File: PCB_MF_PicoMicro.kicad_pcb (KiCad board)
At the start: 2 copper layers, 38 x 18.5 mm, 32 parts, among them J2 Conn_01x02_Pin, J3 USB_C_Receptacle_USB2.0_16P, J7 Conn_01x02_Pin, J8 Conn_01x02_Pin, U1 RP2040, U2 AMS1117-3.3, U4 W25Q16JVSS, U5 ProMicro, Y1 X322512MSB4SI

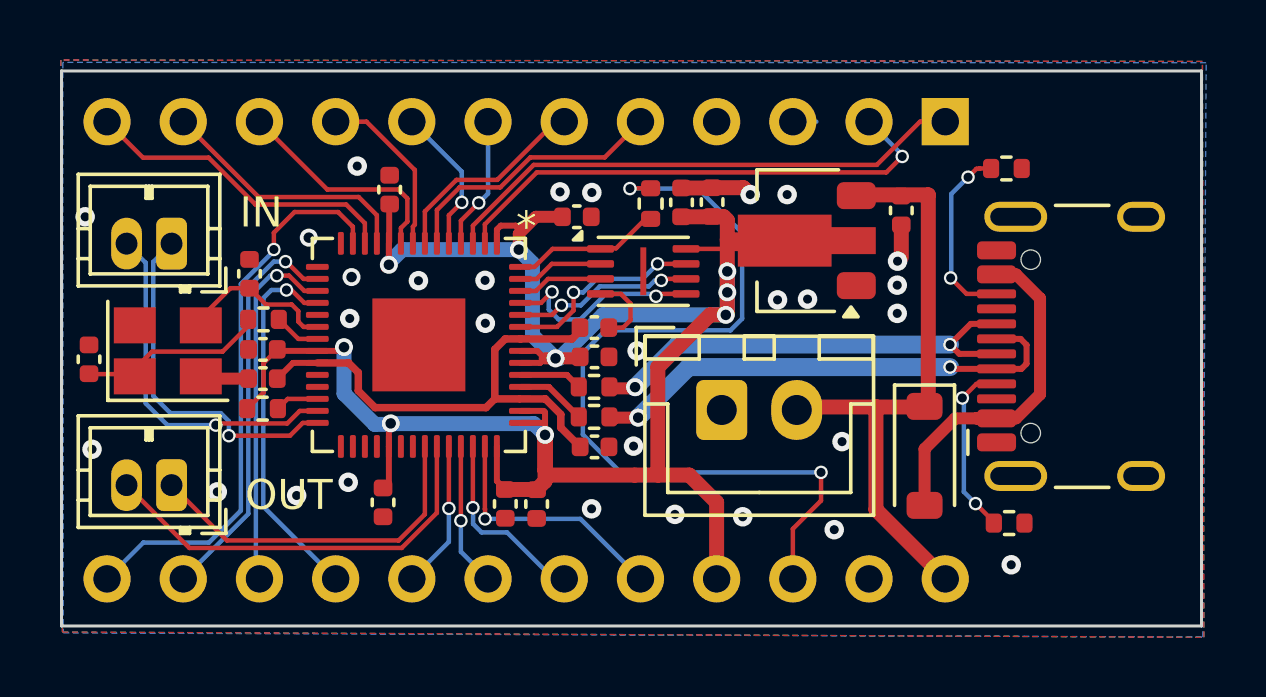
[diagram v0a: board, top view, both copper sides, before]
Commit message: first changes for RP2350A
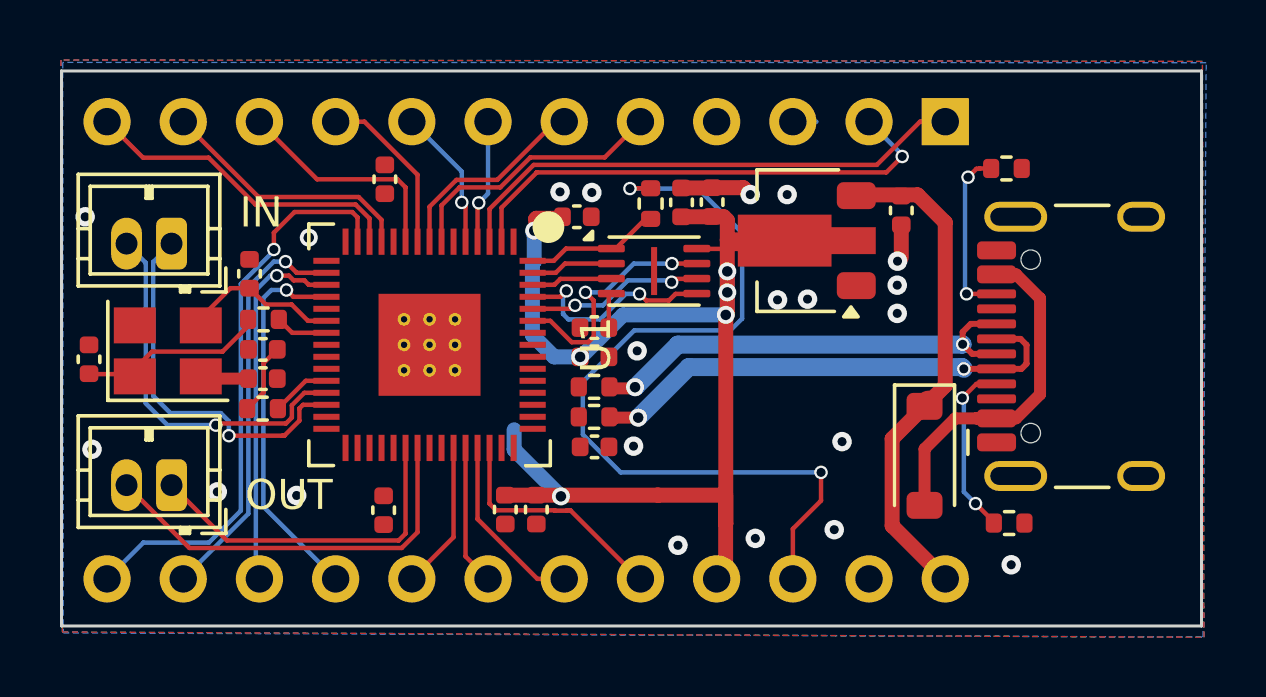
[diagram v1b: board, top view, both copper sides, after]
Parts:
- removed J2: Conn_01x02_Pin, Connector_JST:JST_XH_B2B-XH-A_1x02_P2.50mm_Vertical
- U1: footprint _Neil:QFN56P40_700X700X90L40X18T310N -> _Own_Library:RP2350A_QFN-60_EP_7.75x7.75_Pitch0.4mm
- moved C13 0.38 mm to (116.0, 85.0)
- moved U4 0.36 mm to (125.0, 88.1)
- moved U1 0.36 mm to (117.5, 90.5), turned to -90 degrees
- moved C11 0.26 mm to (116.0, 96.1)
- moved C9 0.19 mm to (120.0, 96.0)
- moved C10 0.18 mm to (121.1, 96.0)
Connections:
- U1 pad 10: 3.3V -> D7
- U1 pad 11: D8 -> 3.3V
- U1 pad 12: D9 -> D8
- U1 pad 13: D10 -> D9
- U1 pad 14: /RP2040/GPIO11 -> D10
- U1 pad 15: /RP2040/GPIO12 -> /RP2040/GPIO11
- U1 pad 16: D13 -> /RP2040/GPIO12
- U1 pad 17: D14 -> D13
- U1 pad 18: D15 -> D14
- U1 pad 19: GND -> D15
- U1 pad 20: /RP2040/XIN -> 3.3V
- U1 pad 21: /RP2040/XOUT_R -> /RP2040/XIN
- U1 pad 22: 3.3V -> /RP2040/XOUT_R
- U1 pad 30: /RP2040/GPIO19 -> 3.3V
- U1 pad 31: /RP2040/GPIO20 -> /RP2040/GPIO19
- U1 pad 32: /RP2040/GPIO21 -> /RP2040/GPIO20
- U1 pad 33: 3.3V -> /RP2040/GPIO21
- U1 pad 38: A0 -> 3.3V
- U1 pad 39: A1 -> +1V1
- U1 pad 40: A2 -> A0
- U1 pad 41: A3 -> A1
- U1 pad 42: 3.3V -> A2
- U1 pad 43: 3.3V -> A3
- U1 pad 45: +1V1 -> 3.3V
- U1 pad 46: /RP2040/USB_D_R- -> unconnected-(U1-VREG_AVDD-Pad46)
- U1 pad 47: /RP2040/USB_D_R+ -> unconnected-(U1-VREG_PGND-Pad47)
- U1 pad 48: 3.3V -> unconnected-(U1-VREG_LX-Pad48)
- U1 pad 49: 3.3V -> unconnected-(U1-VREG_VIN-Pad49)
- U1 pad 50: +1V1 -> unconnected-(U1-VREG_FB-Pad50)
- U1 pad 51: /RP2040/QSPI_SD3 -> /RP2040/USB_D_R-
- U1 pad 52: /RP2040/QSPI_SCLK -> /RP2040/USB_D_R+
- U1 pad 53: /RP2040/QSPI_SD0 -> 3.3V
- U1 pad 54: /RP2040/QSPI_SD2 -> 3.3V
- U1 pad 55: /RP2040/QSPI_SD1 -> /RP2040/QSPI_SD3
- U1 pad 56: /RP2040/QSPI_SS -> /RP2040/QSPI_SCLK
- U1 pad 57: GND -> /RP2040/QSPI_SD0
- U1 pad 6: D4 -> +1V1
- U1 pad 7: D5 -> D4
- U1 pad 8: D6 -> D5
- U1 pad 9: D7 -> D6
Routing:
- net 3.3V: track 79.8 -> 50.5 mm, vias 9 -> 6
- net +1V1: track 17.2 -> 0.00 mm
- net VIN: track 19.9 -> 16.1 mm
- net /RP2040/USB_D_R-: track 2.43 -> 0.08 mm
- net /RP2040/USB_D_R+: track 2.11 -> 0.00 mm
- net GND: track 8.94 -> 7.59 mm, vias 29 -> 21
- net /RP2040/QSPI_SD3: track 6.74 -> 7.75 mm
- net TX1: track 11.8 -> 12.6 mm
- net RX1: track 11.8 -> 12.6 mm
- net BOOT_SEL: track 28.8 -> 28.2 mm
- net /RP2040/~{RST}: track 1.45 -> 2.00 mm
- net A3: track 8.42 -> 7.94 mm, vias 1 -> 0
- net A1: track 4.82 -> 4.71 mm, vias 1 -> 0
- net A2: track 6.02 -> 6.09 mm, vias 1 -> 0
- net A0: track 4.93 -> 4.94 mm, vias 1 -> 0

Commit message: power supply lines routed
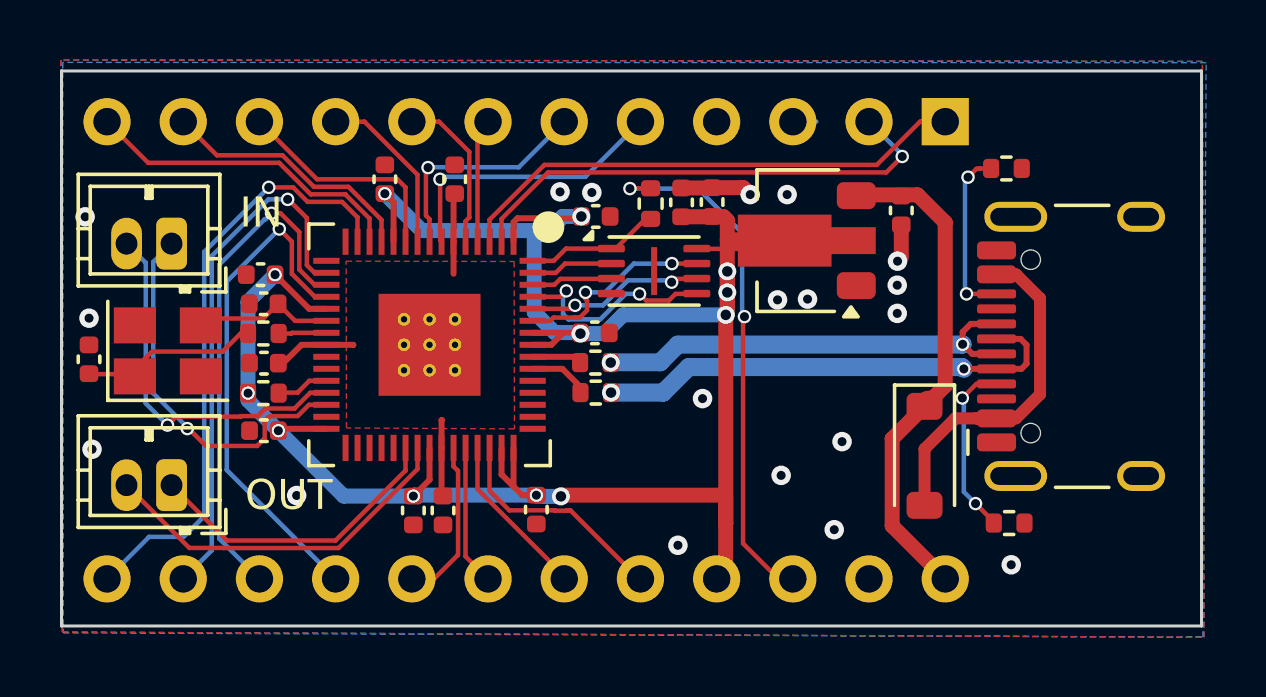
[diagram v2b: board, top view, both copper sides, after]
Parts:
- moved C9 11.3 mm to (111.9, 88.2), turned to 180 degrees
- moved C6 6.79 mm to (118.3, 85.0), turned to 90 degrees
- moved C8 5.48 mm to (118.0, 96.1), turned to -90 degrees
- moved C12 2.71 mm to (112.0, 93.4)
- moved C4 1.10 mm to (112.0, 89.2), turned to 180 degrees
- moved C11 0.99 mm to (117.0, 96.1)
- moved R4 0.81 mm to (123.0, 92.1)
- moved R3 0.81 mm to (123.0, 91.1)
- moved C15 0.80 mm to (123.0, 90.2)
- moved C14 0.63 mm to (123.0, 86.3)
- moved C7 0.52 mm to (112.0, 91.2)
- moved R6 0.52 mm to (112.0, 92.2)
- moved R2 0.47 mm to (112.0, 90.2)
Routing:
- net 3.3V: track 50.5 -> 82.4 mm, vias 6 -> 12
- net BOOT_SEL: track 28.2 -> 17.6 mm
- net +1V1: track 0.00 -> 8.07 mm
- net D14: track 12.8 -> 17.4 mm
- net D15: track 12.8 -> 17.0 mm
- net D13: track 13.8 -> 17.7 mm
- net GND: track 7.59 -> 5.30 mm, vias 21 -> 19
- net /RP2040/USB_D_R-: track 0.08 -> 2.03 mm
- net /RP2040/USB_D_R+: track 0.00 -> 1.66 mm
- net /RP2040/QSPI_SD3: track 7.75 -> 6.33 mm
- net TX2: track 11.7 -> 10.5 mm
- net RX2: track 13.9 -> 12.6 mm
- net D5: track 6.83 -> 8.02 mm, vias 0 -> 1
- net D10: track 19.1 -> 20.1 mm
- net D3: track 4.74 -> 5.38 mm, vias 1 -> 0
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- added copper zone on F.Cu, net +1V1

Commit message: fixed all warnings/errors
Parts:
- C10, C8: value 1uF -> 100nF
- C7: value 100n -> 4.7uF
- moved C12 0.18 mm to (112.0, 93.6)
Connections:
- U1 pad 61: unconnected-(U1-GND-Pad61) -> GND
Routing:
- net GND: track 5.30 -> 7.97 mm, vias 19 -> 26
- net 3.3V: track 82.4 -> 84.2 mm
- net D5: track 8.02 -> 7.33 mm
- net D4: track 10.1 -> 9.51 mm
- net D15: track 17.0 -> 17.5 mm
- net RX1: track 12.7 -> 12.2 mm

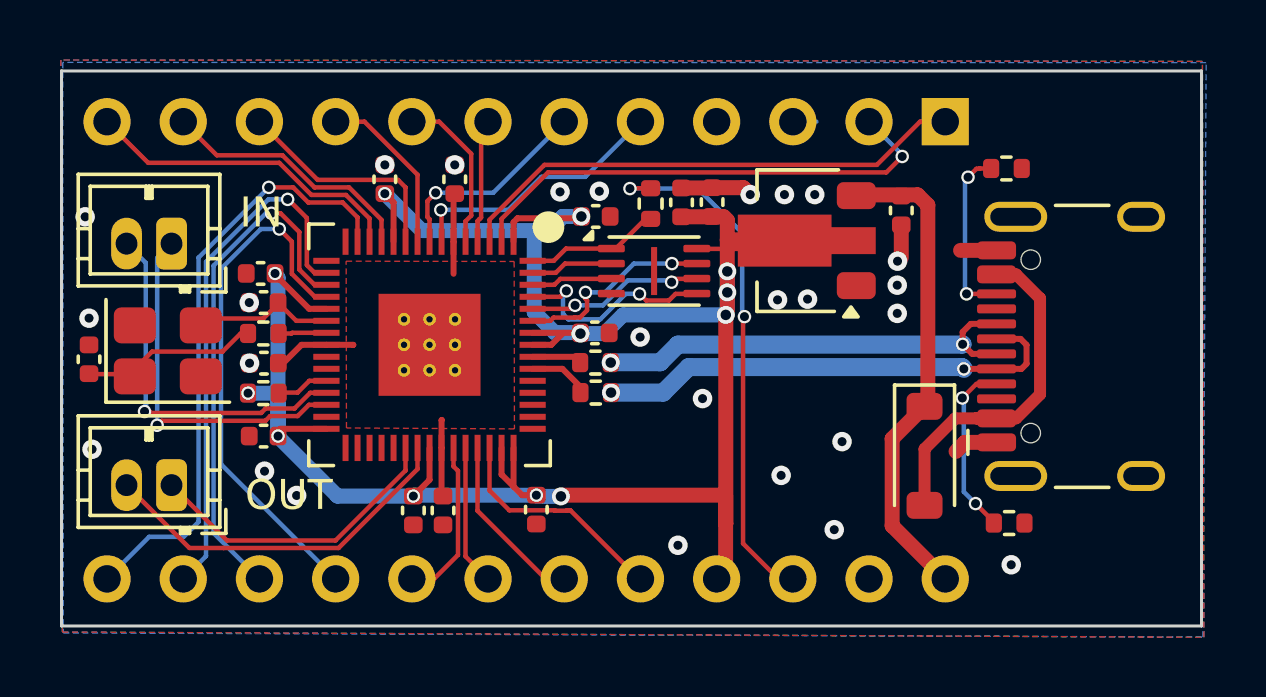
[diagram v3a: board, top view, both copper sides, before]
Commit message: add parts for 1.1V regulator
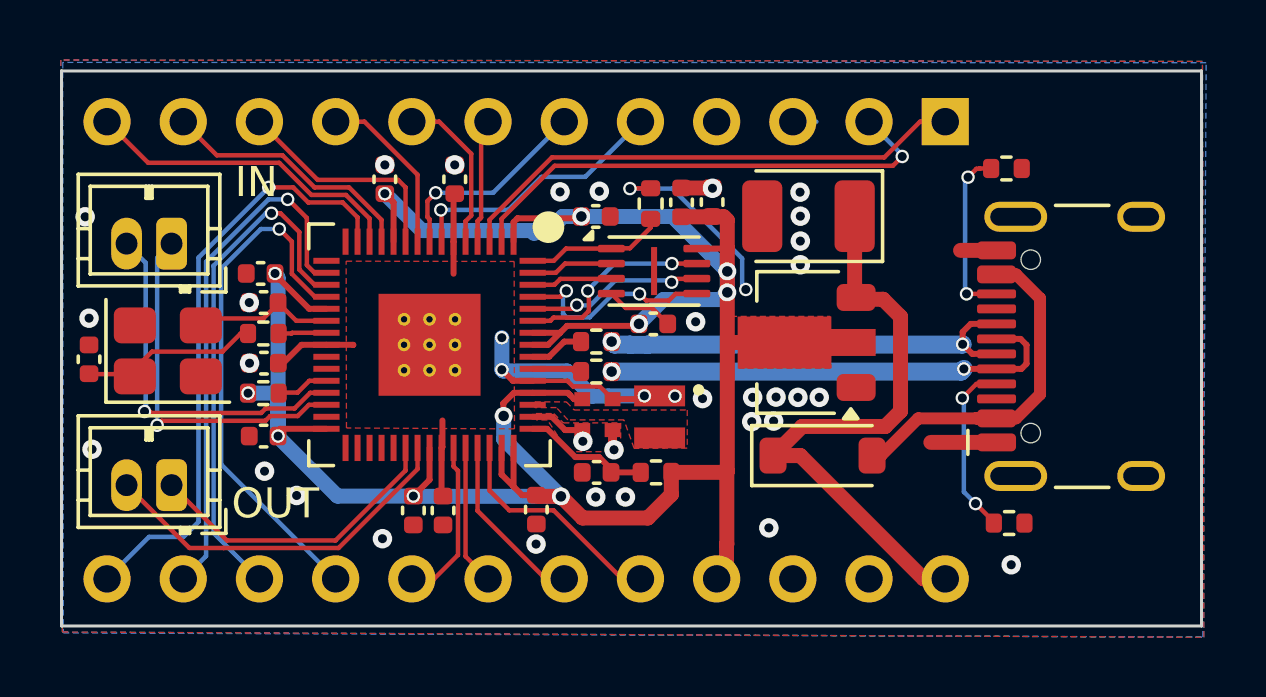
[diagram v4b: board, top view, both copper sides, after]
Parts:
- removed C1: 10u, Capacitor_SMD:C_0402_1005Metric
- added C16: 4.7u, _Own_Library:C_0402_1005Metric_small_pads, F.Cu at (122.6, 92.9)
- added C17: 4.7u, _Own_Library:C_0402_1005Metric_small_pads, F.Cu at (123.6, 92.9)
- added C18: 4.7u, Capacitor_SMD:C_0402_1005Metric, F.Cu at (123.1, 94.8)
- added C19: 47u, Capacitor_Tantalum_SMD:CP_EIA-3528-21_Kemet-B, F.Cu at (130.1, 86.3)
- added L1: 3.3u, _Own_Library:L_pol_2016, F.Cu at (125.2, 93.0)
- added R5: 33, Resistor_SMD:R_0402_1005Metric, F.Cu at (125.0, 94.8)
- moved D1 3.40 mm to (130.6, 94.2), turned to 0 degrees
- moved U2 3.40 mm to (129.8, 90.5)
- moved C15 1.97 mm to (125.0, 89.8)
- moved R3 0.70 mm to (123.1, 90.4)
- moved R4 0.70 mm to (123.1, 91.4)
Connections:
- U1 pad 46: unconnected-(U1-VREG_AVDD-Pad46) -> Net-(U1-VREG_AVDD)
- U1 pad 47: unconnected-(U1-VREG_PGND-Pad47) -> GND
- U1 pad 48: unconnected-(U1-VREG_LX-Pad48) -> /RP2040/VREG_LX
- U1 pad 49: unconnected-(U1-VREG_VIN-Pad49) -> 3.3V
- U1 pad 50: unconnected-(U1-VREG_FB-Pad50) -> +1V1
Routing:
- net +1V1: track 8.07 -> 21.5 mm, vias 0 -> 4
- net BOOT_SEL: track 17.6 -> 6.96 mm
- net VIN: track 15.7 -> 20.1 mm
- net Net-(U1-VREG_AVDD): track 0.00 -> 4.27 mm
- net 3.3V: track 84.2 -> 87.6 mm, vias 12 -> 11
- net GND: track 7.97 -> 10.8 mm, vias 26 -> 32
- added copper zone on F.Cu, net /RP2040/VREG_LX
- added copper zone on F.Cu, net 3.3V

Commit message: optimazations
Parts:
- removed C19: 47u, Capacitor_Tantalum_SMD:CP_EIA-3528-21_Kemet-B
- added C1: 10uF, Capacitor_SMD:C_0402_1005Metric, F.Cu at (130.5, 85.3)
- added SW1: SW_Push, Button_Switch_SMD:SW_Push_1P1T_NO_Vertical_Wuerth_434133025816, F.Cu at (129.7, 95.4)
- moved D1 7.19 mm to (130.2, 87.1)
- moved U2 0.45 mm to (129.7, 90.9)
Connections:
- net /RP2040/GPIO11 renamed /RP2350A/GPIO11
- net /RP2040/GPIO12 renamed /RP2350A/GPIO12
- net /RP2040/GPIO18 renamed /RP2350A/GPIO18
- net /RP2040/GPIO19 renamed /RP2350A/GPIO19
- net /RP2040/GPIO20 renamed /RP2350A/GPIO20
- net /RP2040/GPIO21 renamed /RP2350A/GPIO21
- net /RP2040/GPIO22 renamed /RP2350A/GPIO22
- net /RP2040/GPIO23 renamed /RP2350A/GPIO23
- net /RP2040/QSPI_SCLK renamed /RP2350A/QSPI_SCLK
- net /RP2040/QSPI_SD0 renamed /RP2350A/QSPI_SD0
- net /RP2040/QSPI_SD1 renamed /RP2350A/QSPI_SD1
- net /RP2040/QSPI_SD2 renamed /RP2350A/QSPI_SD2
- net /RP2040/QSPI_SD3 renamed /RP2350A/QSPI_SD3
- net /RP2040/QSPI_SS renamed /RP2350A/QSPI_SS
- net /RP2040/RAW renamed /RP2350A/RAW
- net /RP2040/SWCLK renamed /RP2350A/SWCLK
- net /RP2040/SWD renamed /RP2350A/SWD
- net /RP2040/USB_D+ renamed /RP2350A/USB_D+
- net /RP2040/USB_D- renamed /RP2350A/USB_D-
- net /RP2040/USB_D_R+ renamed /RP2350A/USB_D_R+
- net /RP2040/USB_D_R- renamed /RP2350A/USB_D_R-
- net /RP2040/VREG_LX renamed /RP2350A/VREG_LX
- net /RP2040/XIN renamed /RP2350A/XIN
- net /RP2040/XOUT renamed /RP2350A/XOUT
- net /RP2040/XOUT_R renamed /RP2350A/XOUT_R
- net /RP2040/~{RST} renamed /RP2350A/~{RST}
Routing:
- net BOOT_SEL: track 6.96 -> 27.9 mm
- net VIN: track 20.1 -> 27.8 mm, vias 0 -> 3
- net /RP2350A/RAW: track 12.1 -> 16.6 mm
- net 3.3V: track 87.6 -> 86.2 mm
- net GND: vias 32 -> 22

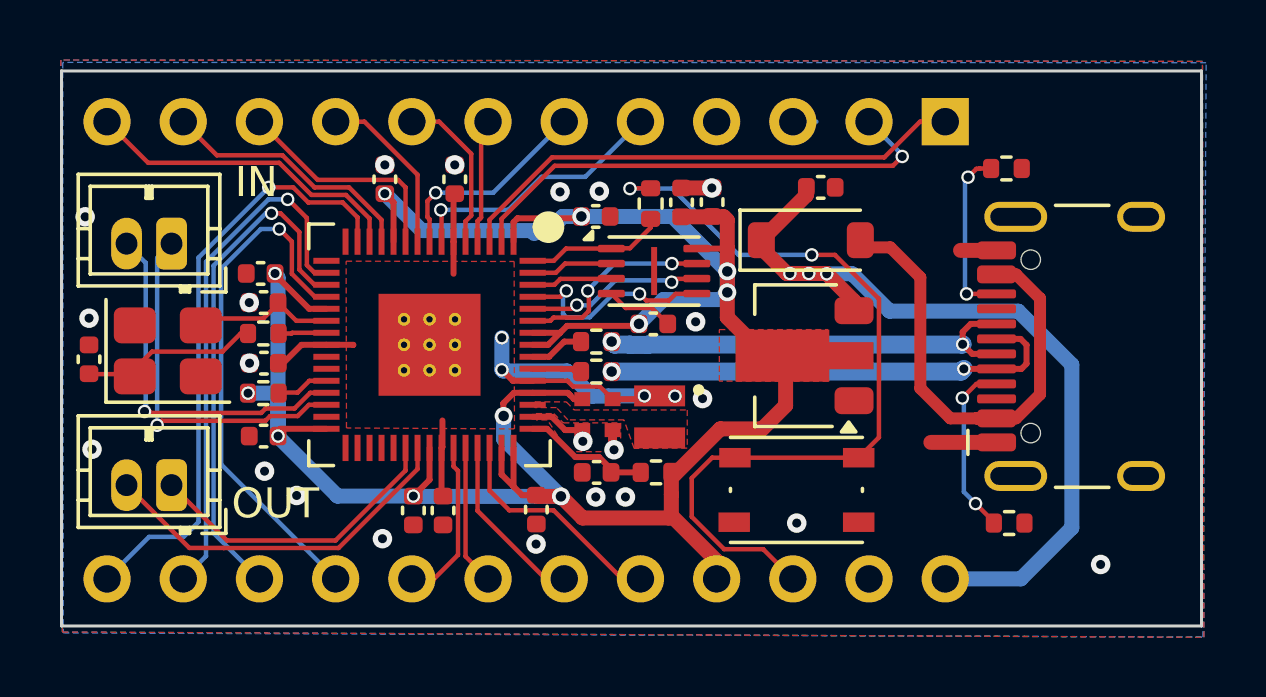
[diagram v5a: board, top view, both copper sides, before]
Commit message: add LED, make board smaller
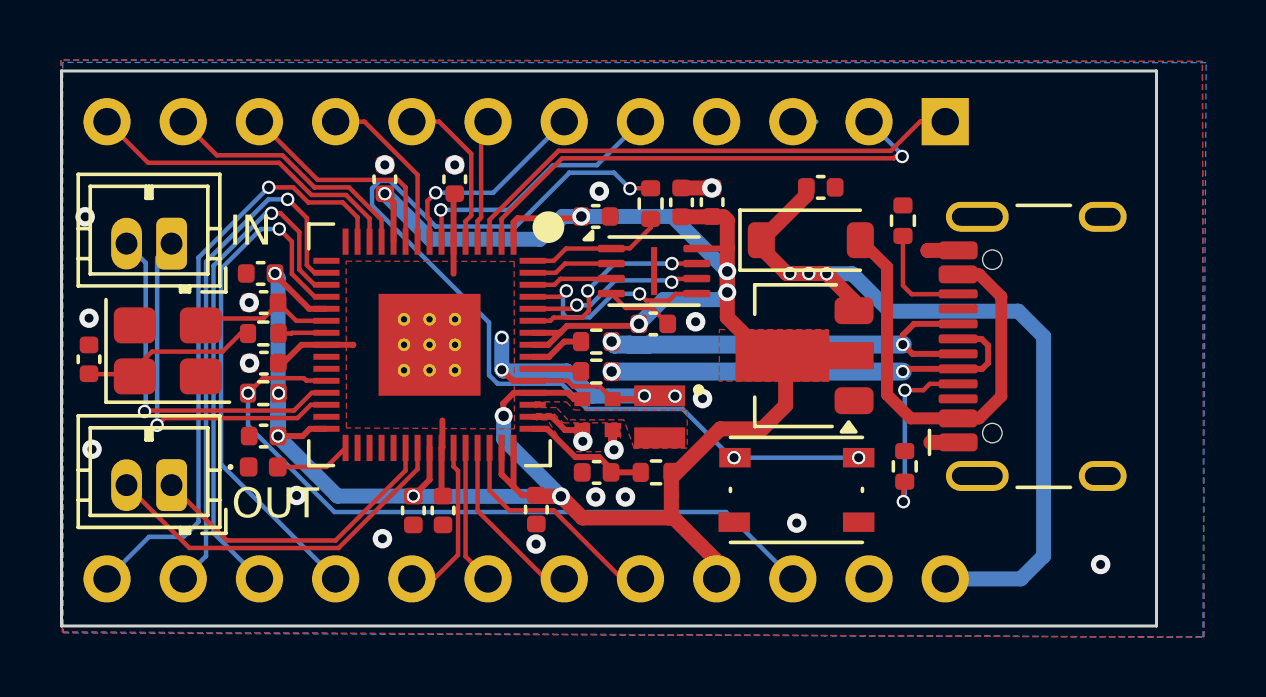
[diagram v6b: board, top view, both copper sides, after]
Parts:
- added D2: LED_Small, LED_SMD:LED_0402_1005Metric, F.Cu at (112.0, 94.6)
- moved R7 3.96 mm to (133.3, 94.6), turned to -90 degrees
- moved R8 3.86 mm to (133.3, 86.4), turned to -90 degrees
- moved J3 1.28 mm to (138.9, 90.6)
- turned R6 to 180 degrees
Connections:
- net /RP2350A/XOUT renamed Net-(C5-Pad1)
- R1 pad 2: BOOT_SEL -> /RP2350A/~{USB_BOOT}
- R6 pad 2: /RP2350A/~{RST} -> RST
- SW1 pad 2: BOOT_SEL -> /RP2350A/~{USB_BOOT}
- U1 pad 26: /RP2350A/~{RST} -> RST
- U5 pad 22: BOOT_SEL -> RST
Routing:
- net /RP2350A/~{USB_BOOT}: track 0.00 -> 32.3 mm, vias 0 -> 3
- net BOOT_SEL: track 27.9 -> 0.00 mm, vias 2 -> 0
- net RST: track 0.00 -> 24.7 mm, vias 0 -> 1
- net /RP2350A/GPIO19: track 0.00 -> 2.52 mm
- net Net-(J3-CC2): track 5.84 -> 3.61 mm, vias 2 -> 0
- net /RP2350A/USB_D-: track 16.2 -> 14.3 mm
- net /RP2350A/~{RST}: track 1.76 -> 0.00 mm
- net /RP2350A/RAW: track 16.6 -> 15.0 mm
- net GND: track 10.8 -> 9.30 mm, vias 22 -> 20
- net 3.3V: track 86.2 -> 84.8 mm
- net VIN: track 27.8 -> 27.0 mm
- net /RP2350A/USB_D+: track 14.8 -> 14.2 mm
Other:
- board size 38 x 18.5 mm -> 36.5 x 18.5 mm
- board text added: "PicoMicro V1.0 08/25"
- board text added: "RST"
- board text removed: "5V"
- board text removed: "BS"
- board text removed: "RP2040MicroMF V2.1-05/25"

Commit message: add 2nd LED
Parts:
- added D3: green, LED_SMD:LED_0402_1005Metric, F.Cu at (111.9, 86.2)
- D2: value LED_Small -> green
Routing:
- net /RP2350A/GPIO11: track 0.00 -> 3.12 mm
- net D13: track 17.7 -> 16.0 mm
- net /RP2350A/~{USB_BOOT}: track 32.3 -> 33.8 mm
- net D14: track 17.7 -> 16.3 mm
- net D15: track 17.5 -> 16.4 mm
- net GND: track 9.30 -> 10.3 mm, vias 20 -> 21
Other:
- board text added: "PicoMicroMS V1.0 08/25"
- board text removed: "PicoMicro V1.0 08/25"
